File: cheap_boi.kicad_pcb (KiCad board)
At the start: 2 copper layers, 120 parts, among them SW1 SW_Push, U1 ATmega32U4-AU, Y1 16MHz

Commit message: everything added besides cutout and usb-connector
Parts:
- C1, C2, C5, C6, C7, F1, R1, R2, R3, R4: moved to B.Cu
- moved C1 130.8 mm to (112.9, 58.7)
- moved C2 125.1 mm to (112.9, 62.7)
- moved C5 114.5 mm to (112.7, 67.5)
- moved C6 114.5 mm to (88.8, 57.9)
- moved F1 109.4 mm to (97.8, 77.8)
- moved R2 108.4 mm to (88.9, 62.7)
- moved USB1 104.7 mm to (100.0, 37.3), turned to 270 degrees
- moved R1 103.6 mm to (88.9, 68.3)
- moved C7 101.0 mm to (112.7, 72.2)
- moved R3 96.9 mm to (88.8, 73.8)
- moved R4 94.8 mm to (104.9, 77.8)
- moved SW1 86.3 mm to (88.1, 39.7)
- moved D2 39.7 mm to (81.0, 65.9)
- moved D3 39.7 mm to (81.0, 85.0)
- moved D1 39.7 mm to (81.0, 46.8)
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
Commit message: last commit of the day
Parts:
- C1, C2, C3, C4, C5, C6, C7, F1, R1, R2, R3, R4, U1, Y1: moved to F.Cu
- moved R1 12.7 mm to (89.0, 55.6)
- moved C6 7.94 mm to (88.9, 65.9), turned to 180 degrees
- moved C4 3.97 mm to (94.5, 50.0), turned to 270 degrees
- moved C3 3.27 mm to (108.7, 49.9), turned to 90 degrees
- moved U1 3.27 mm to (101.6, 61.9)
- moved C2 3.27 mm to (113.7, 59.5)
- moved F1 3.27 mm to (98.6, 74.6)
- moved R4 3.27 mm to (105.7, 74.6)
- moved C1 3.27 mm to (113.7, 55.6)
- moved C5 3.27 mm to (113.5, 64.3)
- moved C7 3.27 mm to (113.5, 69.1)
- moved Y1 2.94 mm to (100.8, 50.3), turned to 90 degrees
- moved R3 2.39 mm to (88.9, 71.4)
- moved R2 2.39 mm to (89.0, 60.3)
- moved USB1 0.79 mm to (100.8, 37.3)
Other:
- board outline added: 287.3 x 76.2 mm

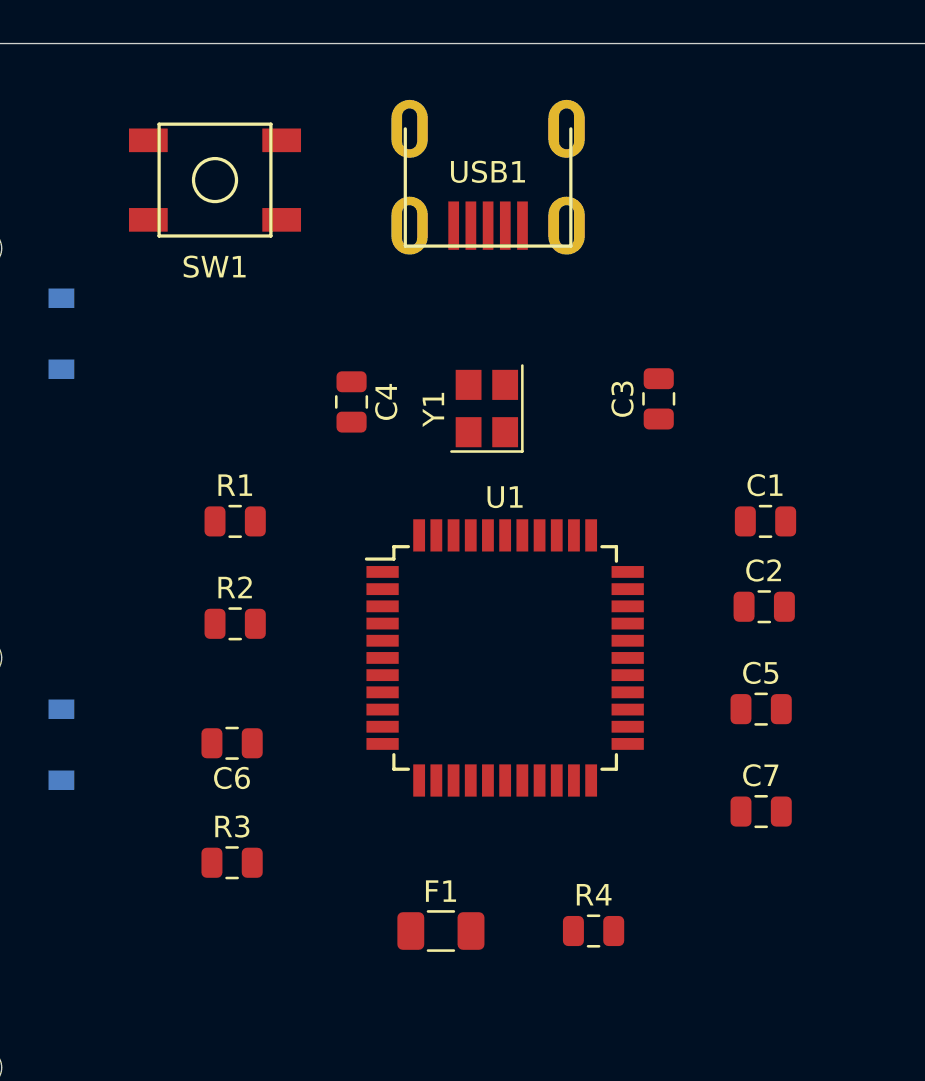
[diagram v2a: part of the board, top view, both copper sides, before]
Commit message: add SSD1306-128x64 submodule
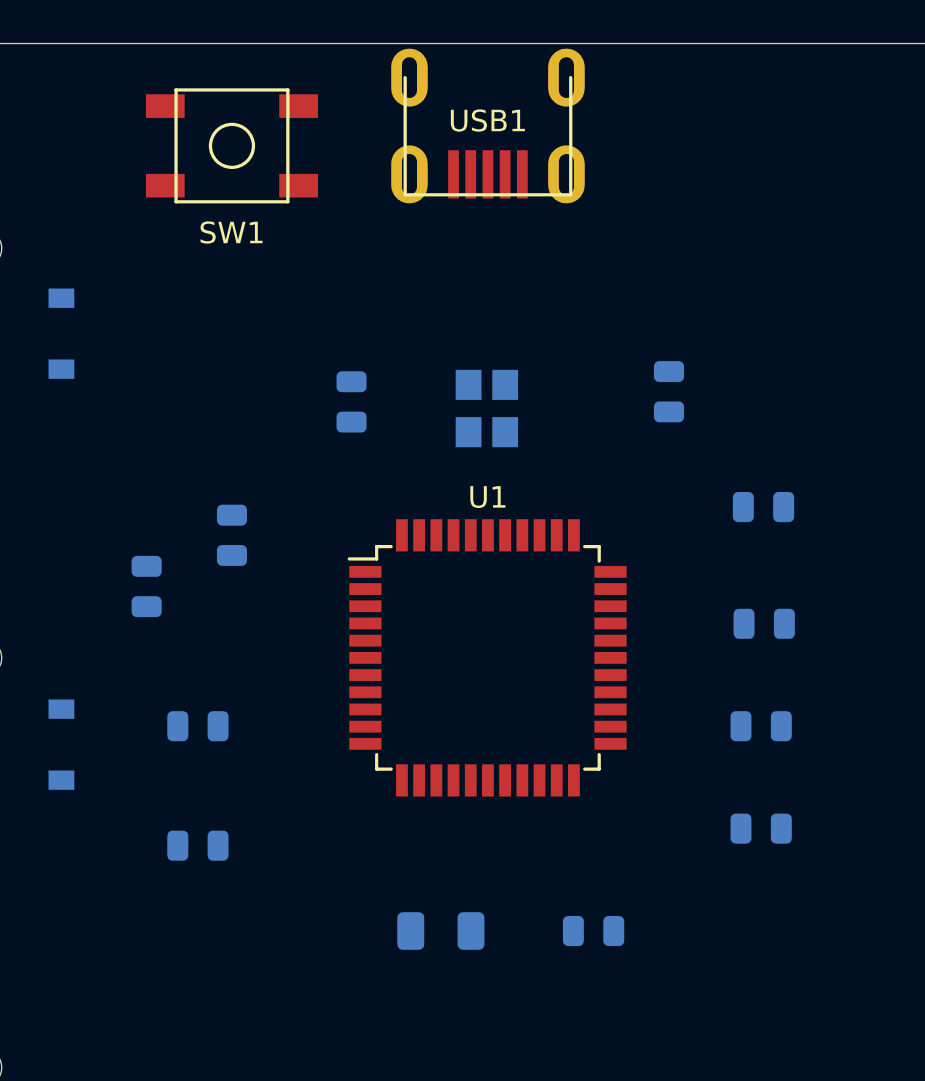
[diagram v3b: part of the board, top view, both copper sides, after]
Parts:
- C1, C2, C3, C4, C5, C6, C7, F1, R1, R2, R3, R4, Y1: moved to B.Cu
- moved R2 4.47 mm to (84.9, 58.6), turned to 270 degrees
- moved USB1 2.38 mm to (100.8, 34.9)
- moved C6 1.77 mm to (87.3, 65.1)
- moved R3 1.77 mm to (87.3, 70.6)
- moved SW1 1.77 mm to (88.9, 38.1)
- moved U1 0.80 mm to (100.8, 61.9)
- moved C2 0.79 mm to (113.7, 60.3)
- moved C5 0.79 mm to (113.5, 65.1)
- moved C7 0.79 mm to (113.5, 69.8)
- moved C1 0.67 mm to (113.6, 54.9)
- moved R1 0.66 mm to (88.9, 56.2), turned to 270 degrees
- moved C3 0.58 mm to (109.2, 49.5), turned to 270 degrees
- turned C4 to 90 degrees
- turned Y1 to 270 degrees

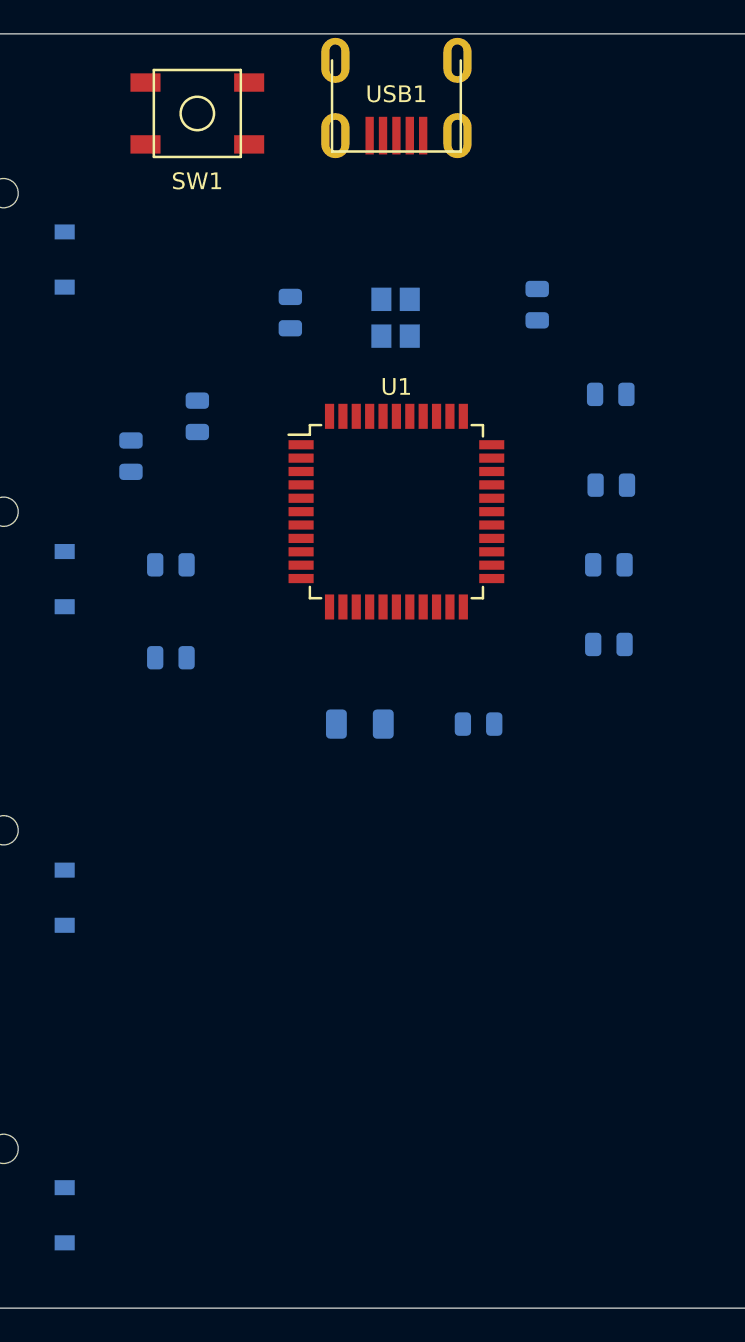
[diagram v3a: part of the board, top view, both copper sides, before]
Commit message: added RGB breakout and ordered parts in symmetrically
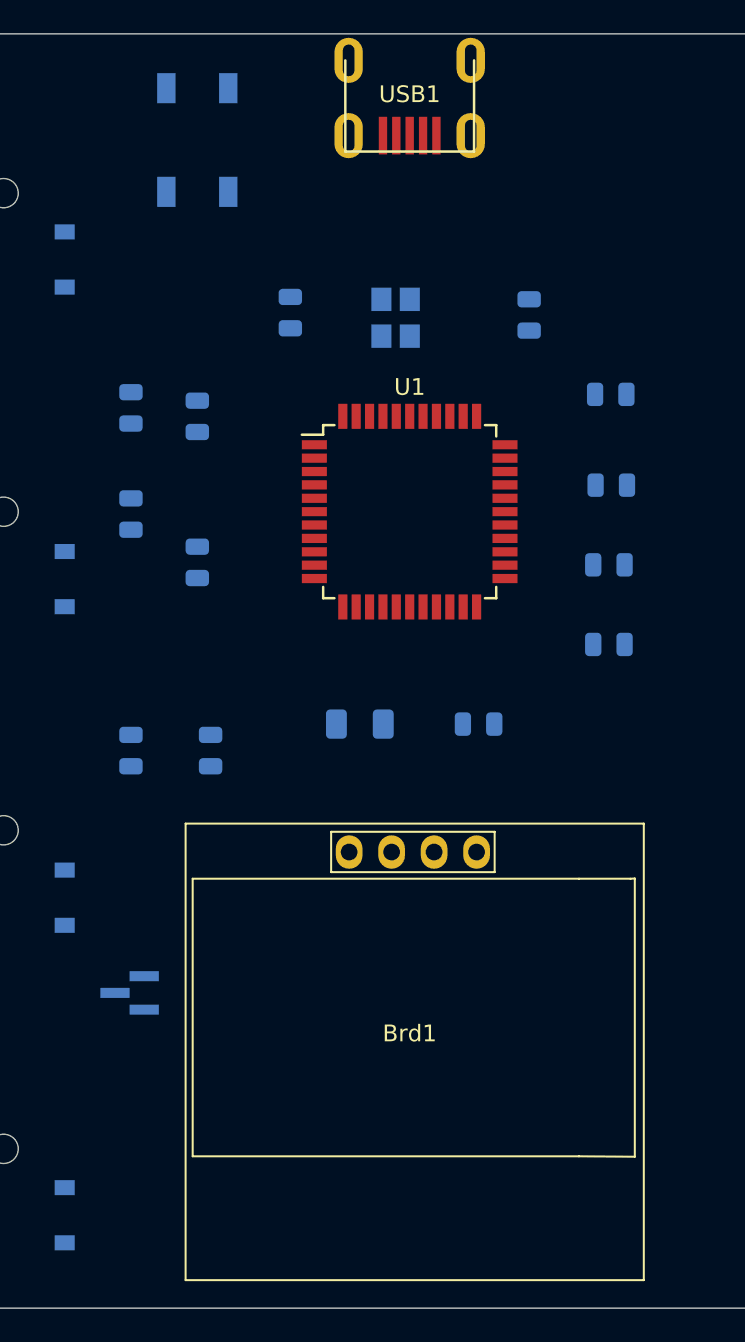
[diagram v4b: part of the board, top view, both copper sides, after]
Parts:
- added Brd1: SSD1306, SSD1306:128x64OLED, F.Cu at (101.6, 92.9)
- added J1: RGB_breakout, Connector_PinHeader_1.00mm:PinHeader_1x03_P1.00mm_Vertical_SMD_Pin1Left, B.Cu at (84.8, 90.7)
- added R5: 4.7k, Resistor_SMD:R_0805_2012Metric, B.Cu at (84.9, 76.2)
- added R6: 4.7k, Resistor_SMD:R_0805_2012Metric, B.Cu at (89.7, 76.2)
- SW1: moved to B.Cu
- moved R3 5.92 mm to (88.9, 64.9), turned to 90 degrees
- moved C6 3.86 mm to (84.9, 62.1), turned to 90 degrees
- moved R2 2.89 mm to (84.9, 55.7)
- moved SW1 1.59 mm to (88.9, 39.7), turned to 270 degrees
- moved U1 0.79 mm to (101.6, 61.9)
- moved USB1 0.79 mm to (101.6, 34.9)
- moved C3 0.78 mm to (108.7, 50.1)
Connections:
- U1 pad 18: Net-(U1-Pad18) -> SCL
- U1 pad 19: Net-(U1-Pad19) -> SDA

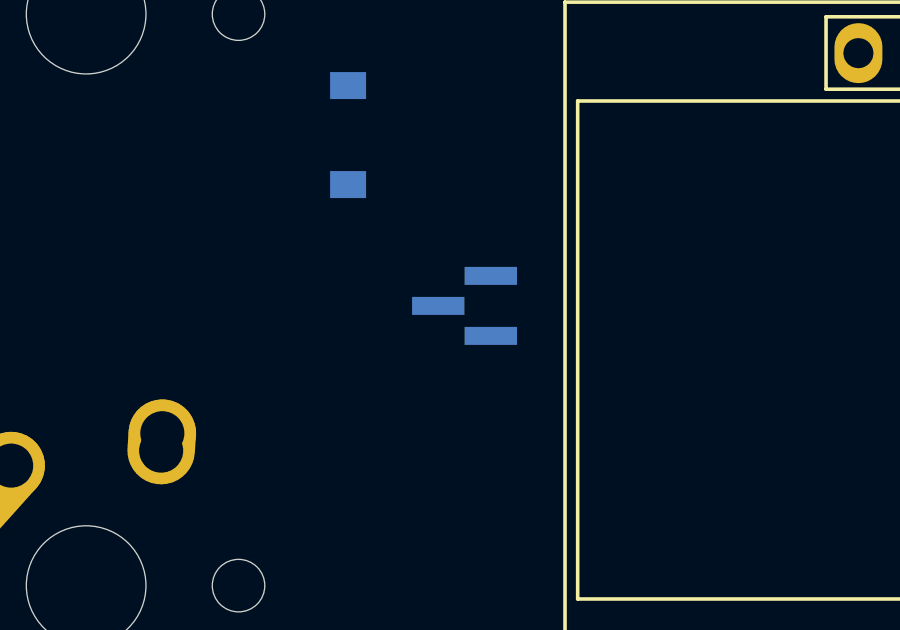
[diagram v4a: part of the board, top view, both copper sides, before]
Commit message: added connection of rows and cols to microcontroller
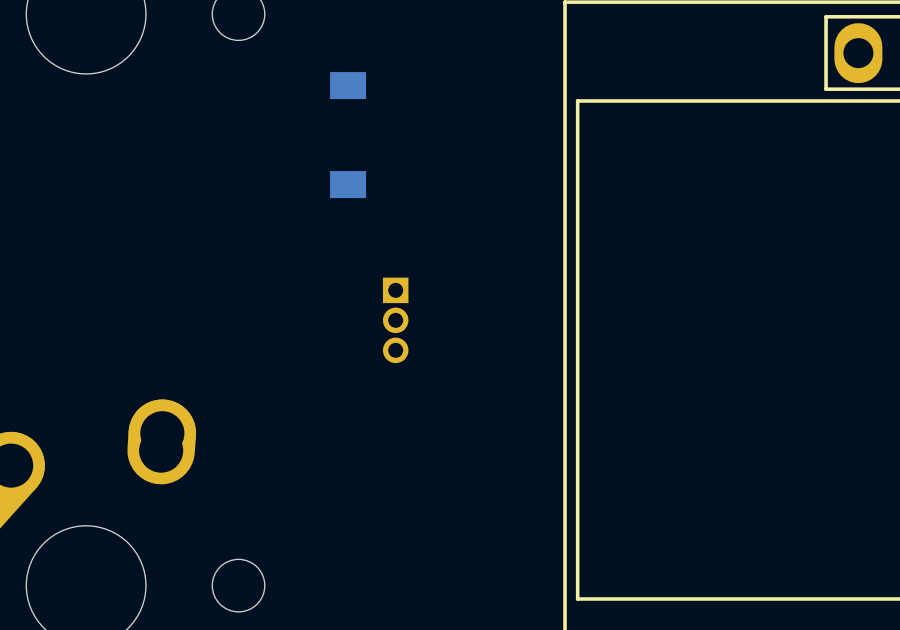
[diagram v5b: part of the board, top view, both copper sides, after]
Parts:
- J1: footprint Connector_PinHeader_1.00mm:PinHeader_1x03_P1.00mm_Vertical_SMD_Pin1Left -> Connector_PinHeader_1.00mm:PinHeader_1x03_P1.00mm_Vertical
- moved J1 2.35 mm to (82.5, 90.2)
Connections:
- U1 pad 1: Net-(U1-Pad1) -> COL0
- U1 pad 20: Net-(U1-Pad20) -> ROW1
- U1 pad 21: Net-(U1-Pad21) -> ROW2
- U1 pad 22: Net-(U1-Pad22) -> ROW3
- U1 pad 25: Net-(U1-Pad25) -> COL1
- U1 pad 26: Net-(U1-Pad26) -> COL2
- U1 pad 27: Net-(U1-Pad27) -> COL3
- U1 pad 28: Net-(U1-Pad28) -> COL4
- U1 pad 29: Net-(U1-Pad29) -> COL5
- U1 pad 30: Net-(U1-Pad30) -> COL6
- U1 pad 31: Net-(U1-Pad31) -> COL7
- U1 pad 32: Net-(U1-Pad32) -> COL8
- U1 pad 36: Net-(U1-Pad36) -> ROW0
- U1 pad 37: Net-(U1-Pad37) -> COL9
- U1 pad 38: Net-(U1-Pad38) -> COL10
- U1 pad 39: Net-(U1-Pad39) -> COL11
- U1 pad 40: Net-(U1-Pad40) -> COL12

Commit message: tracing is done, PCB should be functional
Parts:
- added REF**: MountingHole_5.3mm_M5, MountingHole:MountingHole_5.3mm_M5, F.Cu at (331.0, 71.5)
- added REF**: MountingHole_5.3mm_M5, MountingHole:MountingHole_5.3mm_M5, F.Cu at (236.0, 71.5)
- added REF**: MountingHole_5.3mm_M5, MountingHole:MountingHole_5.3mm_M5, F.Cu at (140.5, 71.5)
- added REF**: MountingHole_5.3mm_M5, MountingHole:MountingHole_5.3mm_M5, F.Cu at (82.0, 71.5)
- moved R5 27.6 mm to (112.4, 74.7), turned to 0 degrees
- moved C4 23.5 mm to (97.8, 73.3), turned to 270 degrees
- moved C3 23.3 mm to (105.5, 73.2), turned to 90 degrees
- moved R6 23.3 mm to (112.4, 71.1), turned to 0 degrees
- moved Y1 22.9 mm to (101.6, 73.2), turned to 180 degrees
- moved F1 22.5 mm to (101.9, 52.3), turned to 180 degrees
- moved C1 20.7 mm to (93.0, 56.1), turned to 90 degrees
- moved C7 18.7 mm to (106.7, 52.5)
- moved R4 18.7 mm to (111.9, 57.0), turned to 270 degrees
- moved C2 18.4 mm to (96.8, 52.8)
- moved D2 5.47 mm to (81.5, 60.5)
- moved C6 5.13 mm to (90.0, 61.7)
- moved R3 3.34 mm to (90.2, 68.0)
- moved R2 2.67 mm to (85.3, 58.3)
- moved SW1 2.36 mm to (88.6, 37.3), turned to 0 degrees
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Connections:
- U1 pad 8: Net-(U1-Pad8) -> Din1
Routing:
- net COL12: track 0.00 -> 367.9 mm, vias 0 -> 4
- net COL11: track 0.00 -> 347.7 mm, vias 0 -> 4
- net COL10: track 0.00 -> 322.7 mm, vias 0 -> 2
- net ROW3: track 0.00 -> 321.7 mm, vias 0 -> 1
- net ROW2: track 0.00 -> 310.8 mm, vias 0 -> 1
- net ROW1: track 0.00 -> 305.8 mm, vias 0 -> 2
- net COL9: track 0.00 -> 300.0 mm, vias 0 -> 2
- net ROW0: track 0.00 -> 288.7 mm, vias 0 -> 3
- net COL8: track 0.00 -> 261.6 mm, vias 0 -> 2
- net COL7: track 0.00 -> 238.6 mm, vias 0 -> 2
- net COL6: track 0.00 -> 198.1 mm
- net COL5: track 0.00 -> 177.9 mm
- net GND: track 0.00 -> 167.7 mm, vias 0 -> 7
- net COL4: track 0.00 -> 158.8 mm
- net COL3: track 0.00 -> 139.7 mm
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- added copper zone on B.Cu, net GND
- added copper zone on F.Cu, net GND
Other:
- net class Power added: clearance 0.2, trace_width 0.381, via_dia 0.8, via_drill 0.4

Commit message: silkscreen text, GND fill, error checking
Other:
- board text added: "cheap_boi Rev 1 made by MangoIV, thx to the 40% Discord server for excessive help"

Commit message: added RGB underglow, removed 3 pin breakout for RGB underglow
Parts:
- removed J1: RGB_breakout, Connector_PinHeader_1.00mm:PinHeader_1x03_P1.00mm_Vertical
- added D53: WS2812B, LED_SMD:LED_WS2812B_PLCC4_5.0x5.0mm_P3.2mm, B.Cu at (81.8, 90.4)
- added D54: WS2812B, LED_SMD:LED_WS2812B_PLCC4_5.0x5.0mm_P3.2mm, B.Cu at (81.7, 52.3)
- added D55: WS2812B, LED_SMD:LED_WS2812B_PLCC4_5.0x5.0mm_P3.2mm, B.Cu at (140.5, 52.5)
- added D56: WS2812B, LED_SMD:LED_WS2812B_PLCC4_5.0x5.0mm_P3.2mm, B.Cu at (235.7, 52.3)
- added D57: WS2812B, LED_SMD:LED_WS2812B_PLCC4_5.0x5.0mm_P3.2mm, B.Cu at (331.0, 52.3)
- added D58: WS2812B, LED_SMD:LED_WS2812B_PLCC4_5.0x5.0mm_P3.2mm, B.Cu at (331.0, 90.6)
- added D59: WS2812B, LED_SMD:LED_WS2812B_PLCC4_5.0x5.0mm_P3.2mm, B.Cu at (235.8, 90.7)
- added D60: WS2812B, LED_SMD:LED_WS2812B_PLCC4_5.0x5.0mm_P3.2mm, B.Cu at (140.5, 90.6)
- added R7: 500, Resistor_SMD:R_0805_2012Metric, B.Cu at (85.6, 79.6)
- moved D51 4.52 mm to (345.1, 86.6), turned to 0 degrees
- moved D52 4.52 mm to (345.1, 105.7), turned to 0 degrees
- moved D50 4.41 mm to (345.2, 66.0), turned to 0 degrees
- moved D49 4.33 mm to (345.3, 48.6), turned to 0 degrees
- moved D1 3.70 mm to (81.5, 43.2)
- moved D3 3.16 mm to (81.7, 81.9)
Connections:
- U1 pad 8: Din1 -> RGB1
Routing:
- net +5V: track 89.8 -> 660.1 mm, vias 10 -> 12
- net GND: track 167.7 -> 689.5 mm, vias 7 -> 16
- net Net-(D56-Pad2): track 0.00 -> 101.5 mm
- net Net-(D55-Pad2): track 0.00 -> 101.4 mm
- net Net-(D59-Pad2): track 0.00 -> 91.7 mm
- net Net-(D58-Pad2): track 0.00 -> 91.6 mm
- net Net-(D54-Pad2): track 0.00 -> 78.3 mm, vias 0 -> 4
- net Net-(D53-Pad2): track 0.00 -> 73.6 mm
- net Net-(D57-Pad2): track 0.00 -> 58.9 mm, vias 0 -> 2
- net Din1: track 34.1 -> 0.00 mm
- net RGB1: track 0.00 -> 20.9 mm, vias 0 -> 1
- net Net-(D53-Pad4): track 0.00 -> 12.9 mm, vias 0 -> 2
- net ROW2: track 310.8 -> 318.6 mm
- net ROW3: track 321.7 -> 315.9 mm
- net ROW1: track 305.8 -> 300.1 mm
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- removed copper zone on B.Cu, net GND
- removed copper zone on F.Cu, net GND
